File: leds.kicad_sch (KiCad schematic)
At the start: 88 parts

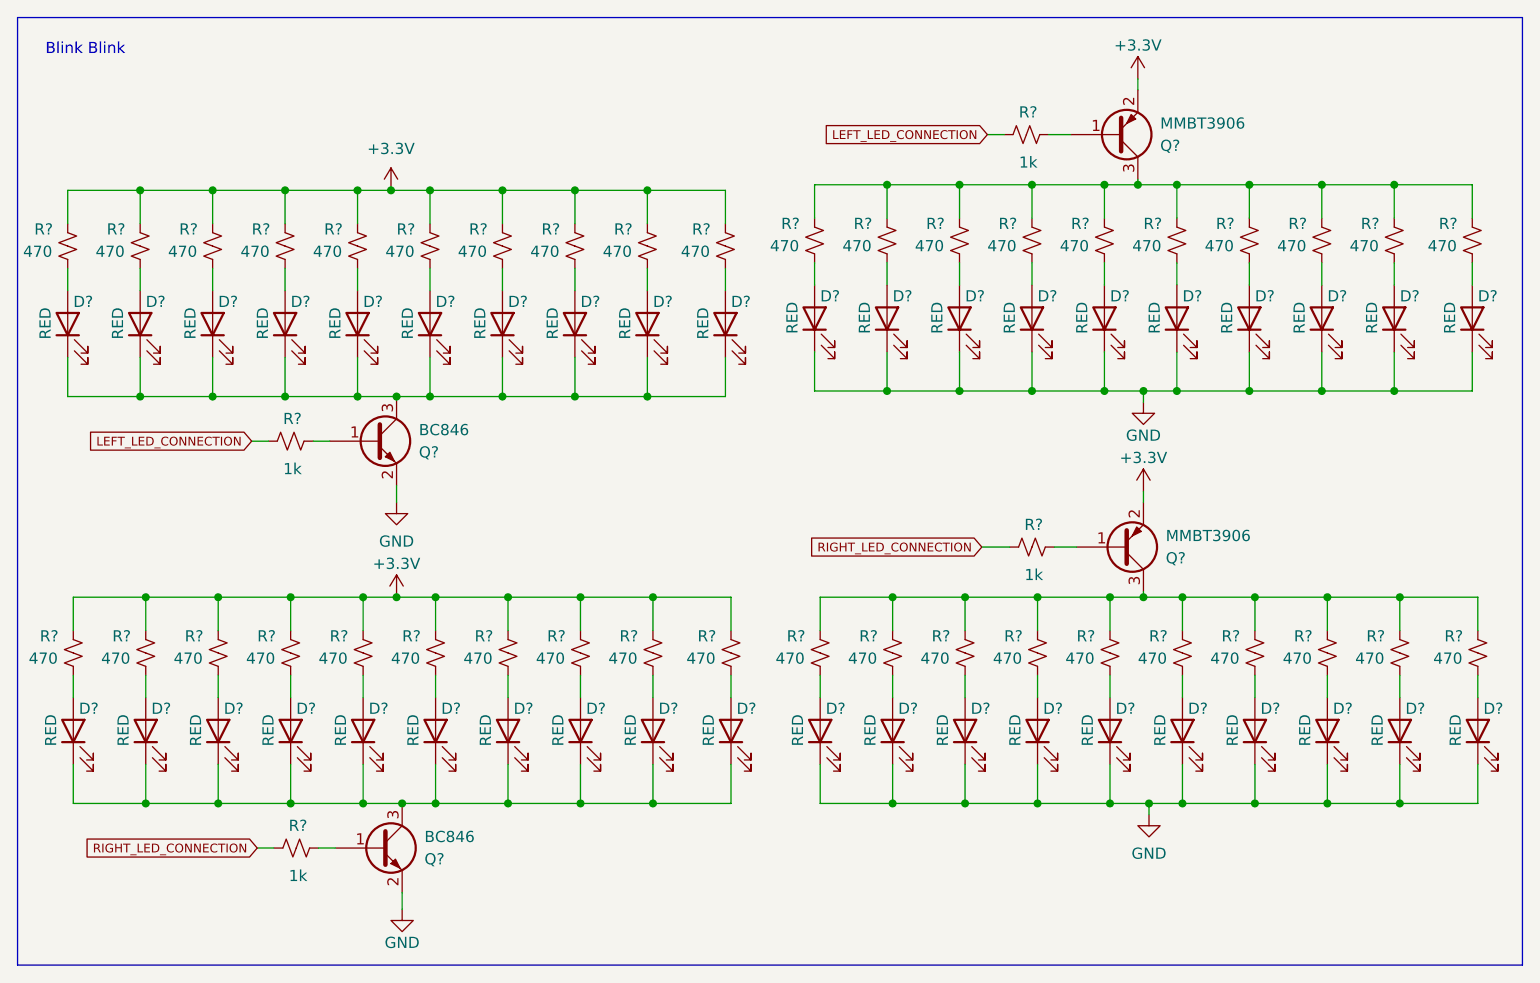
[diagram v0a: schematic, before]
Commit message: Added datasheet for the LED and assigned 3d parts.
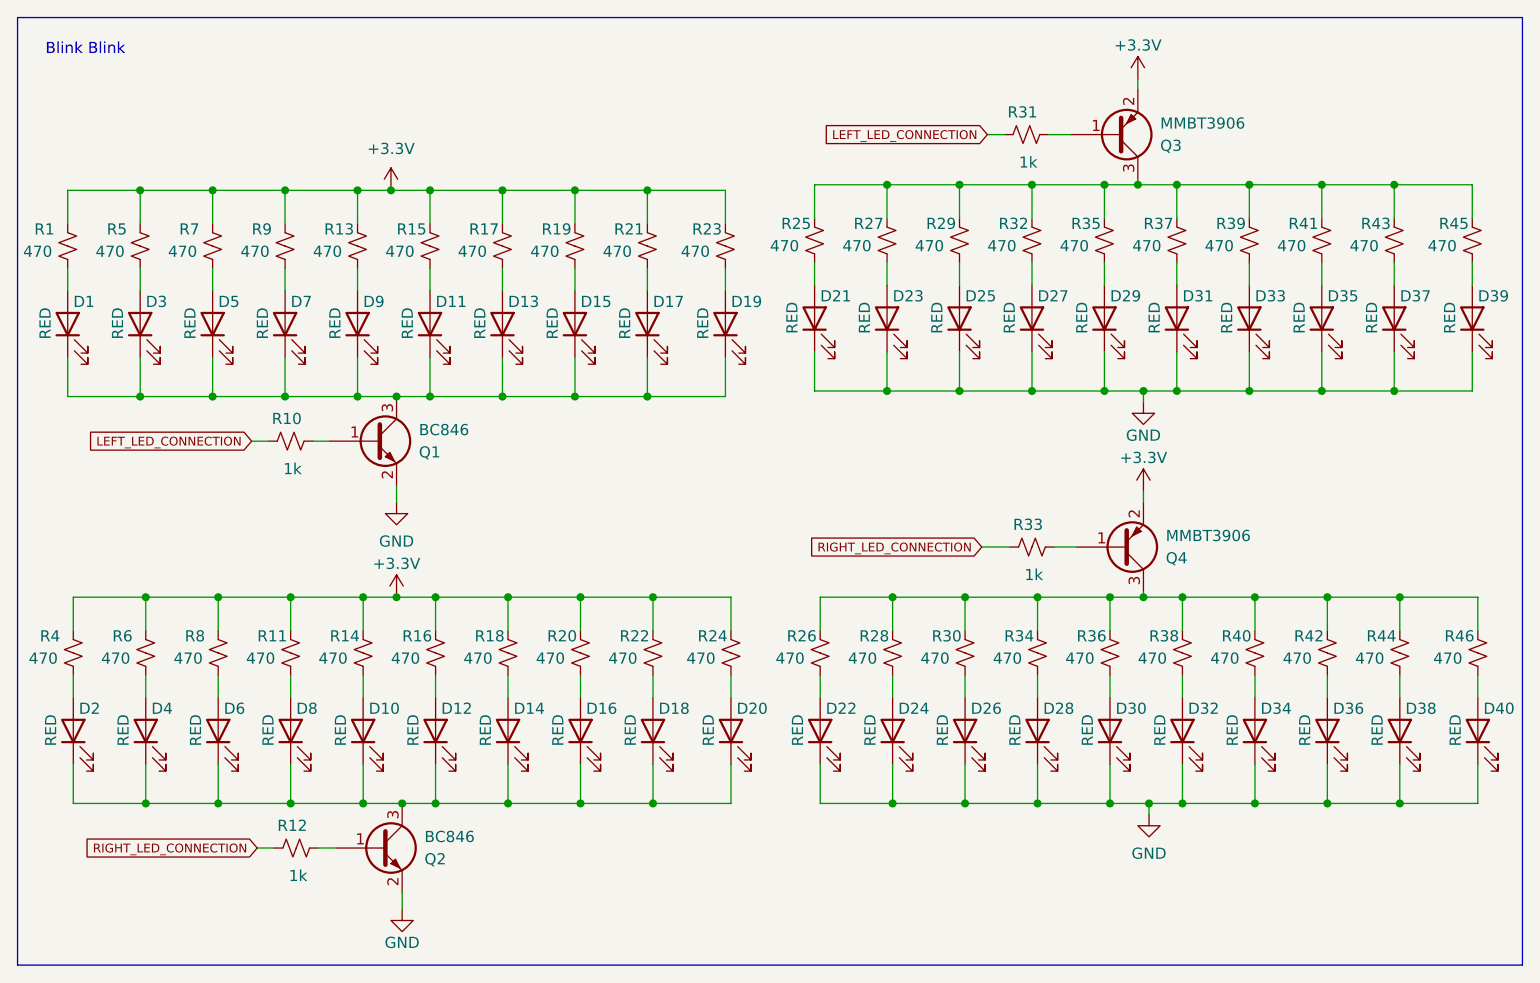
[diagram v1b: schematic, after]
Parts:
- gave numbers to parts that had none: 88
